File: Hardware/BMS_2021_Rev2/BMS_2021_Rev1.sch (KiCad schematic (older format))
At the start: 7 parts, among them U1 TM4C129E_Launchpad

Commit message: BEGAN REWIRING CELL FILTER CIRCUITS
THT tiva, New Schott. diode footprint (pending Lipina approval)
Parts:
- U1: footprint MRDT_Shields:TM4C129E_Launchpad_FULL_SMD_TOP -> MRDT_Shields:TM4C129E_Launchpad_FULL_THT_TOP
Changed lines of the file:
@@
 F 0 "U1" H 7850 1700 60  0000 L CNN
 F 1 "TM4C129E_Launchpad" H 7600 1800 60  0000 L CNN
-F 2 "MRDT_Shields:TM4C129E_Launchpad_FULL_SMD_TOP" H 7800 1850 60  0001 C CNN
+F 2 "MRDT_Shields:TM4C129E_Launchpad_FULL_THT_TOP" H 7800 1850 60  0001 C CNN
 F 3 "" H 7800 1850 60  0001 C CNN
 	1    7800 1850
@@
 F 0 "U1" H 8450 3100 60  0000 C CNN
 F 1 "TM4C129E_Launchpad" H 8600 3000 60  0000 C CNN
-F 2 "MRDT_Shields:TM4C129E_Launchpad_FULL_SMD_TOP" H 8350 1850 60  0001 C CNN
+F 2 "MRDT_Shields:TM4C129E_Launchpad_FULL_THT_TOP" H 8350 1850 60  0001 C CNN
 F 3 "" H 8350 1850 60  0001 C CNN
 	2    8350 1850
@@
 F 0 "U1" H 9225 3025 60  0000 L CNN
 F 1 "TM4C129E_Launchpad" H 8725 3125 60  0000 L CNN
-F 2 "MRDT_Shields:TM4C129E_Launchpad_FULL_SMD_TOP" H 9200 3175 60  0001 C CNN
+F 2 "MRDT_Shields:TM4C129E_Launchpad_FULL_THT_TOP" H 9200 3175 60  0001 C CNN
 F 3 "" H 9200 3175 60  0001 C CNN
 	3    9200 3175
@@
 F 0 "U1" H 9650 4400 60  0000 L CNN
 F 1 "TM4C129E_Launchpad" H 9125 4325 60  0000 L CNN
-F 2 "MRDT_Shields:TM4C129E_Launchpad_FULL_SMD_TOP" H 9750 3175 60  0001 C CNN
+F 2 "MRDT_Shields:TM4C129E_Launchpad_FULL_THT_TOP" H 9750 3175 60  0001 C CNN
 F 3 "" H 9750 3175 60  0001 C CNN
 	4    9750 3175
@@
 F 0 "U1" H 8275 3450 60  0000 C CNN
 F 1 "TM4C129E_Launchpad" H 8425 3350 60  0000 C CNN
-F 2 "MRDT_Shields:TM4C129E_Launchpad_FULL_SMD_TOP" H 8175 3500 60  0001 C CNN
+F 2 "MRDT_Shields:TM4C129E_Launchpad_FULL_THT_TOP" H 8175 3500 60  0001 C CNN
 F 3 "" H 8175 3500 60  0001 C CNN
 	5    8175 3500
@@
 F 0 "U1" H 7650 4450 60  0000 L CNN
 F 1 "TM4C129E_Launchpad" H 7350 4350 60  0000 L CNN
-F 2 "MRDT_Shields:TM4C129E_Launchpad_FULL_SMD_TOP" H 7600 4500 60  0001 C CNN
+F 2 "MRDT_Shields:TM4C129E_Launchpad_FULL_THT_TOP" H 7600 4500 60  0001 C CNN
 F 3 "" H 7600 4500 60  0001 C CNN
 	6    7600 4500
@@
 F 0 "U1" H 9075 5575 60  0000 L CNN
 F 1 "TM4C129E_Launchpad" H 8650 5475 60  0000 L CNN
-F 2 "MRDT_Shields:TM4C129E_Launchpad_FULL_SMD_TOP" H 9050 5625 60  0001 C CNN
+F 2 "MRDT_Shields:TM4C129E_Launchpad_FULL_THT_TOP" H 9050 5625 60  0001 C CNN
 F 3 "" H 9050 5625 60  0001 C CNN
 	7    9050 5625
@@
 F 0 "U1" H 9675 5575 60  0000 L CNN
 F 1 "TM4C129E_Launchpad" H 8900 6775 60  0000 L CNN
-F 2 "MRDT_Shields:TM4C129E_Launchpad_FULL_SMD_TOP" H 9625 5625 60  0001 C CNN
+F 2 "MRDT_Shields:TM4C129E_Launchpad_FULL_THT_TOP" H 9625 5625 60  0001 C CNN
 F 3 "" H 9625 5625 60  0001 C CNN
 	8    9625 5625

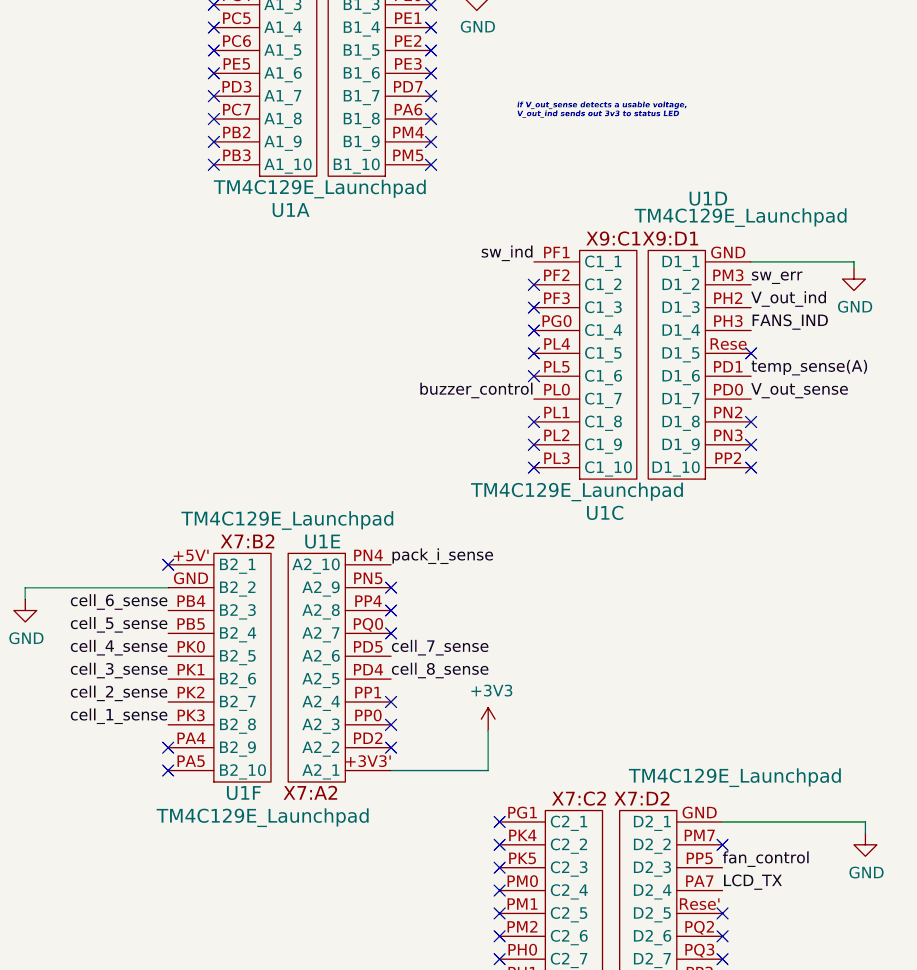
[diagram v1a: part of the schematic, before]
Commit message: New Cell filters complete
In the process of adding diodes for filtering to the tivas
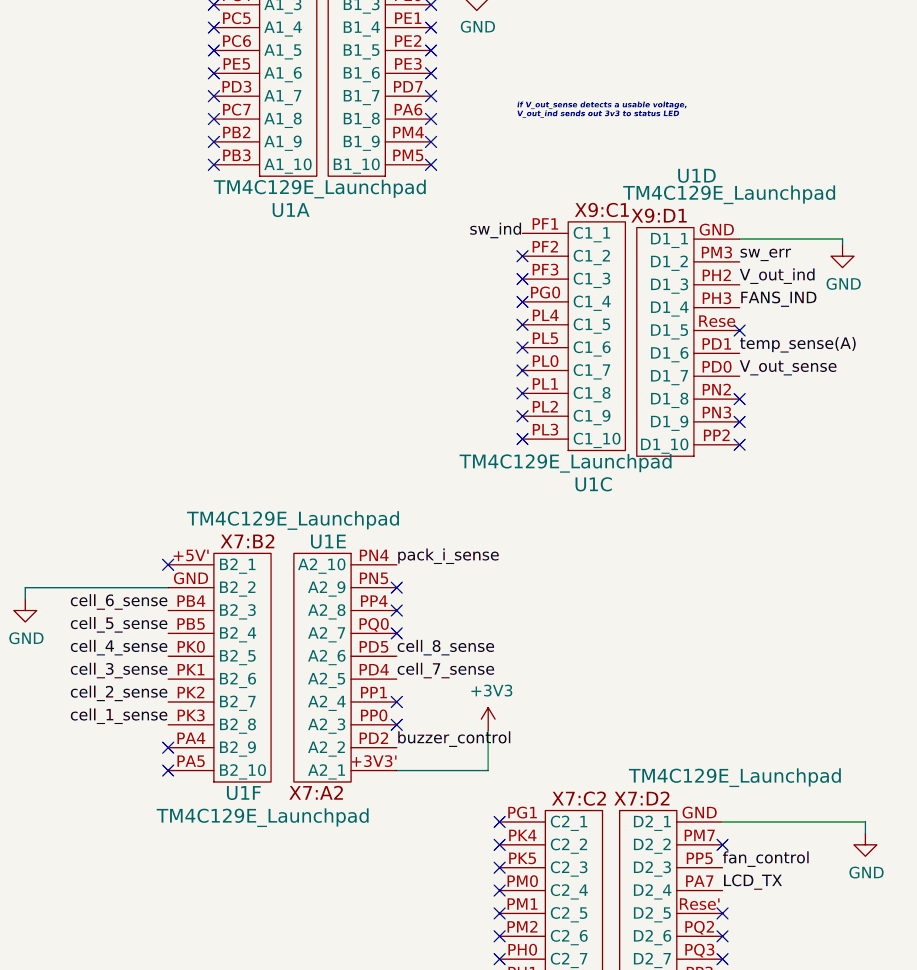
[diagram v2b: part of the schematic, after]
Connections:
- net buzzer_control: now also U1.PD2 (A2_2); no longer U1.PL0 (C1_7)
- net cell_7_sense: now also U1.PD4 (A2_5); no longer U1.PD5 (A2_6)
- net cell_8_sense: now also U1.PD5 (A2_6); no longer U1.PD4 (A2_5)
- net sw_ind: no longer U1.PF1 (C1_1)
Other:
- moved on the sheet: U1C, U1D, U1E
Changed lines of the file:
@@
 Text Label 4200 4750 0    50   ~ 0
 V_out_sense
-Text Label 9950 2825 0    50   ~ 0
+Text Label 9900 2725 0    50   ~ 0
 V_out_sense
 Text Label 3000 4600 2    50   ~ 0
@@
 Text Label 4900 2900 2    50   ~ 0
 buzzer_control
-Text Label 9000 2825 2    50   ~ 0
+Text Label 8400 4350 0    50   ~ 0
 buzzer_control
 Text Label 9825 5575 0    50   ~ 0
 pack_gate
-Text Label 9950 2325 0    50   ~ 0
+Text Label 9900 2225 0    50   ~ 0
 sw_err
-Text Label 9000 2225 2    50   ~ 0
+Text Label 8950 2125 2    50   ~ 0
 sw_ind
-Text Label 9950 2725 0    50   ~ 0
+Text Label 9900 2625 0    50   ~ 0
 temp_sense(A)
-Text Label 9950 2425 0    50   ~ 0
+Text Label 9900 2325 0    50   ~ 0
 V_out_ind
 Text Label 6100 2675 0    50   ~ 0
@@
 Text Notes 8925 1600 0    24   Italic 5
 if V_out_sense detects a usable voltage,\nV_out_ind sends out 3v3 to status LED
-Text Label 9950 2525 0    50   ~ 0
+Text Label 9900 2425 0    50   ~ 0
 FANS_IND
 Text Label 4900 3000 2    50   ~ 0
@@
 L MRDT_Shields:TM4C129E_Launchpad U1
 U 3 1 5FA5E750
-P 9200 3175
-F 0 "U1" H 9225 3025 60  0000 L CNN
-F 1 "TM4C129E_Launchpad" H 8725 3125 60  0000 L CNN
-F 2 "MRDT_Shields:TM4C129E_Launchpad_FULL_THT_TOP" H 9200 3175 60  0001 C CNN
-F 3 "" H 9200 3175 60  0001 C CNN
-	3    9200 3175
+P 9150 3050
+F 0 "U1" H 9175 2900 60  0000 L CNN
+F 1 "TM4C129E_Launchpad" H 8675 3000 60  0000 L CNN
+F 2 "MRDT_Shields:TM4C129E_Launchpad_FULL_THT_TOP" H 9150 3050 60  0001 C CNN
+F 3 "" H 9150 3050 60  0001 C CNN
+	3    9150 3050
 	1    0    0    -1
 $EndComp
@@
 L MRDT_Shields:TM4C129E_Launchpad U1
 U 4 1 5FA60370
-P 9750 3175
-F 0 "U1" H 9650 4400 60  0000 L CNN
-F 1 "TM4C129E_Launchpad" H 9125 4325 60  0000 L CNN
-F 2 "MRDT_Shields:TM4C129E_Launchpad_FULL_THT_TOP" H 9750 3175 60  0001 C CNN
-F 3 "" H 9750 3175 60  0001 C CNN
-	4    9750 3175
+P 9700 3075
+F 0 "U1" H 9600 4300 60  0000 L CNN
+F 1 "TM4C129E_Launchpad" H 9075 4225 60  0000 L CNN
+F 2 "MRDT_Shields:TM4C129E_Launchpad_FULL_THT_TOP" H 9700 3075 60  0001 C CNN
+F 3 "" H 9700 3075 60  0001 C CNN
+	4    9700 3075
 	-1   0    0    -1
 $EndComp
-Text Label 8375 4050 0    50   ~ 0
+Text Label 8400 3950 0    50   ~ 0
 cell_8_sense
-Text Label 8375 3950 0    50   ~ 0
+Text Label 8400 4050 0    50   ~ 0
 cell_7_sense
-NoConn ~ 8375 3750
-NoConn ~ 8375 3850
-NoConn ~ 8375 4150
-NoConn ~ 8375 4250
-NoConn ~ 8375 4350
+NoConn ~ 8400 3750
+NoConn ~ 8400 3850
+NoConn ~ 8400 4150
+NoConn ~ 8400 4250
 $Comp
 L MRDT_Shields:TM4C129E_Launchpad U1
 U 5 1 5F805ECA
-P 8175 3500
-F 0 "U1" H 8275 3450 60  0000 C CNN
-F 1 "TM4C129E_Launchpad" H 8425 3350 60  0000 C CNN
-F 2 "MRDT_Shields:TM4C129E_Launchpad_FULL_THT_TOP" H 8175 3500 60  0001 C CNN
-F 3 "" H 8175 3500 60  0001 C CNN
-	5    8175 3500
+P 8200 3500
+F 0 "U1" H 8300 3450 60  0000 C CNN
+F 1 "TM4C129E_Launchpad" H 8450 3350 60  0000 C CNN
+F 2 "MRDT_Shields:TM4C129E_Launchpad_FULL_THT_TOP" H 8200 3500 60  0001 C CNN
+F 3 "" H 8200 3500 60  0001 C CNN
+	5    8200 3500
 	-1   0    0    1
 $EndComp
@@
 NoConn ~ 8850 4775
 NoConn ~ 8850 4675
-NoConn ~ 9950 2625
-NoConn ~ 9950 2925
-NoConn ~ 9950 3025
-NoConn ~ 9950 3125
-NoConn ~ 9000 3125
-NoConn ~ 9000 3025
-NoConn ~ 9000 2925
-NoConn ~ 9000 2725
-NoConn ~ 9000 2625
-NoConn ~ 9000 2525
-NoConn ~ 9000 2425
-NoConn ~ 9000 2325
+NoConn ~ 9900 2525
+NoConn ~ 9900 2825
+NoConn ~ 9900 2925
+NoConn ~ 9900 3025
+NoConn ~ 8950 3000
+NoConn ~ 8950 2900
+NoConn ~ 8950 2800
+NoConn ~ 8950 2600
+NoConn ~ 8950 2500
+NoConn ~ 8950 2400
+NoConn ~ 8950 2300
+NoConn ~ 8950 2200
 Wire Wire Line
 	2900 925  2950 925
@@
 Wire Notes Line
 	2150 500  2150 4300
-Text Label 8375 3550 0    50   ~ 0
+Text Label 8400 3550 0    50   ~ 0
 pack_i_sense
 NoConn ~ 9825 5475
 NoConn ~ 8550 1400
-NoConn ~ 8375 3650
+NoConn ~ 8400 3650
 NoConn ~ 7600 1300
 NoConn ~ 7600 1000
@@
 $EndComp
 Wire Wire Line
-	9950 2225 10400 2225
-Wire Wire Line
-	10400 2225 10400 2250
+	9900 2125 10350 2125
+Wire Wire Line
+	10350 2125 10350 2150
 $Comp
 L power:GND #PWR0102
 U 1 1 5FD27455
-P 10400 2250
-F 0 "#PWR0102" H 10400 2000 50  0001 C CNN
-F 1 "GND" H 10405 2077 50  0000 C CNN
-F 2 "" H 10400 2250 50  0001 C CNN
-F 3 "" H 10400 2250 50  0001 C CNN
-	1    10400 2250
+P 10350 2150
+F 0 "#PWR0102" H 10350 1900 50  0001 C CNN
+F 1 "GND" H 10355 1977 50  0000 C CNN
+F 2 "" H 10350 2150 50  0001 C CNN
+F 3 "" H 10350 2150 50  0001 C CNN
+	1    10350 2150
 	1    0    0    -1
 $EndComp
@@
 	1    0    0    -1
 $EndComp
-Wire Wire Line
-	8375 4450 8800 4450
 Wire Wire Line
 	2950 925  2950 1225
@@
 Text Label 900  1250 2    50   ~ 0
 V_in
+Wire Wire Line
+	8400 4450 8800 4450
+NoConn ~ 8950 2700
 $EndSCHEMATC

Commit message: REV 2 COMPLETE
Finished Rev 2. Future changes may include silkscreen additions.
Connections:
- net sw_ind: now also U1.PF1 (C1_1)
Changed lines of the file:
@@
 Text Label 9900 2225 0    50   ~ 0
 sw_err
-Text Label 8950 2125 2    50   ~ 0
+Text Label 8950 2100 2    50   ~ 0
 sw_ind
 Text Label 9900 2625 0    50   ~ 0
